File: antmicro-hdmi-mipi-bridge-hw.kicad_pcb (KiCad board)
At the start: 4 copper layers, 68 x 45 mm, 121 parts, among them IC1 TLV73325PDBVT, IC2 TLV73312PDBVT, IC3 TLV73325PDBVT, IC4 TLV73312PDBVT, J2 HDMI-A_Molex_471511001, J4 HDMI-A_Molex_471511001, J6 Conn_FFC_WE_68715014022, U1 TC358743XBG, U2 TPD8S009DSMR, U3 PCA9517ATP, U4 TC358743XBG, U5 TPD8S009DSMR, U6 PCA9517ATP, Y1 Oscillator_27MHz_TXC_7C, Y2 Oscillator_27MHz_TXC_7C

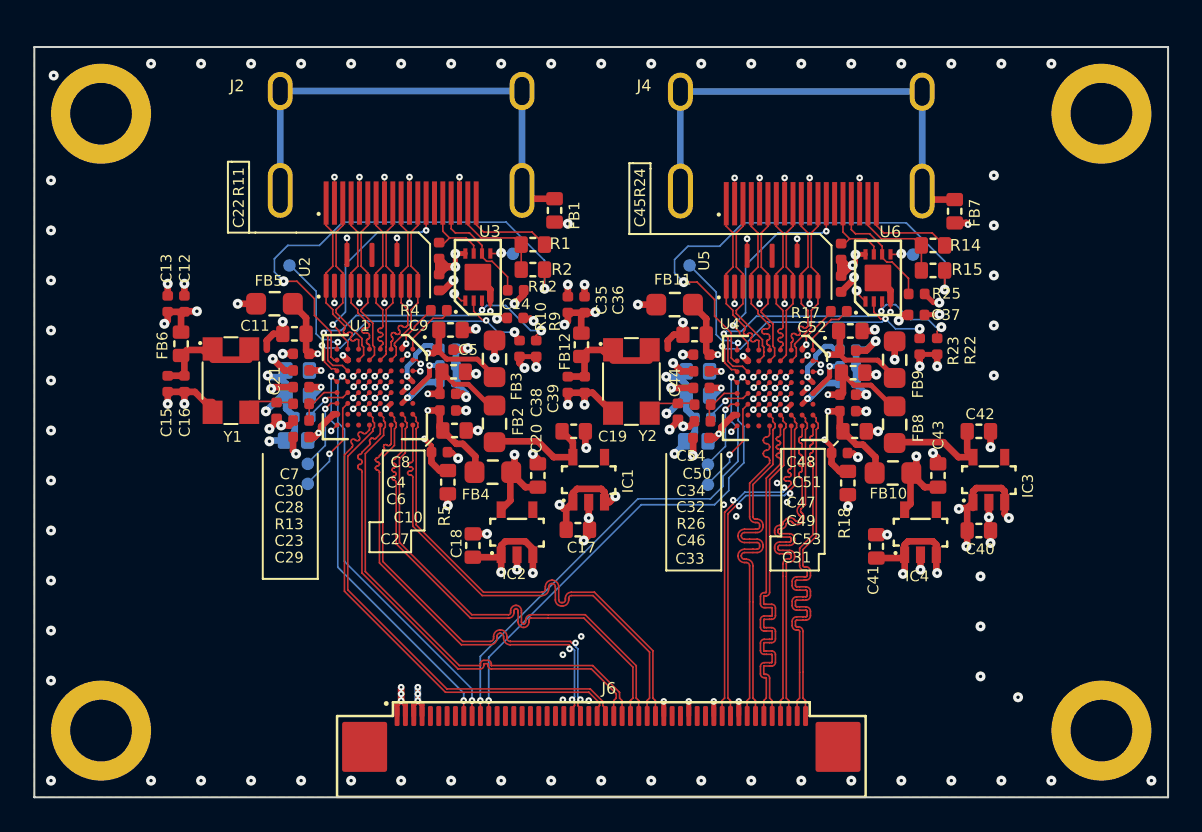
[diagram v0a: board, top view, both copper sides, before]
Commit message: Switch to micro-HDMI and widely-available parts for JLCPCB
- J2/J4: HDMI-A Molex 471511001 -> micro-HDMI (Type D) Molex 467651001,
  KiCad stock footprint. Symbol renumbered to the Type D pinout.
  D2/D0 fan out on F.Cu; D1/CLK drop to B.Cu via 0.15/0.30 mm vias in
  front of the inner pad row and rejoin the original routing, so the
  ESD-to-TC358743 routing is unchanged. Intra-pair skew re-matched to
  0.000 mm on all 8 pairs. DDC/HPD/CEC/5V re-routed for the new pinout.
- U3/U6: PCA9517ATP (HWSON8) -> PCA9517ADP (MSOP-8, same die), moved
  1.45 mm up into the space freed by the smaller connector.
- Y1/Y2: TXC 7C-27.000MBB-T -> HELE SSI027000E3CH; pads moved to the
  datasheet land (+-1.27 mm, previously +-1.9 mm).
- SP1-4: Wurth 9774060151R -> Sinhoo SMTSO2560CTJ; hole 3.7 -> 4.25 mm.
- IC2/IC4: TLV73312PDBVT -> TLV74312PDBVR (same pinout);
  IC1/IC3: TLV73325PDBVT -> TLV73325PDBVR (reel code).
- 470 pF, 4.7 uF, 2 k, 22 R: MPNs updated to in-stock equivalents.
- Design rules: min via diameter 0.40 -> 0.30 mm,
  min copper-to-edge clearance 0 -> 0.25 mm.

DRC: 0 unconnected, 0 schematic parity issues.

Co-Authored-By: Claude Opus 5.5 <noreply@anthropic.com>
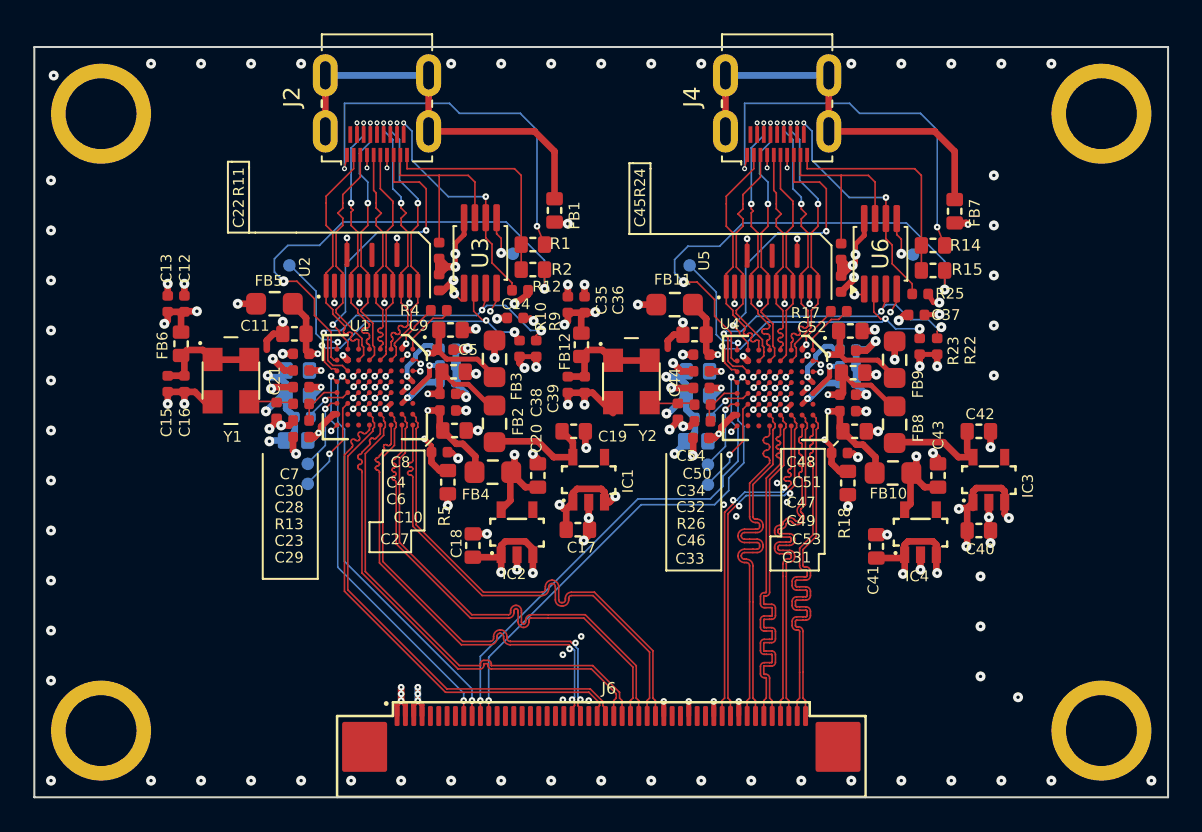
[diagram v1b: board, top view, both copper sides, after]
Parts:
- IC1, IC3: value TLV73325PDBVT -> TLV73325PDBVR
- IC2, IC4: value TLV73312PDBVT -> TLV74312PDBVR
- J2, J4: value HDMI-A_Molex_471511001 -> HDMI-D_Molex_467651001; footprint antmicro-footprints:HDMI-A_Receptacle_Molex_471511001 -> Connector_Video:HDMI_Micro-D_Molex_46765-1xxx
- SP1, SP2, SP3, SP4: value Spacer_Drill3.7mm_H6mm_9774060151R -> Spacer_Drill4.25mm_H6mm_SMTSO2560CTJ; footprint antmicro-footprints:Spacer_Drill3.7mm_H6mm_9774060151R -> antmicro-footprints:Spacer_Drill4.25mm_H6mm_SMTSO2560CTJ
- U3, U6: value PCA9517ATP -> PCA9517ADP; footprint antmicro-footprints:SOT1069-2 -> Package_SO:MSOP-8_3x3mm_P0.65mm
- Y1, Y2: value Oscillator_27MHz_TXC_7C -> Oscillator_27MHz_HELE_SSI027000E3CH
- moved J4 3.01 mm to (159.6, 91.7)
- moved J2 2.98 mm to (135.6, 91.7)
- moved U6 1.46 mm to (165.8, 102.4), turned to 90 degrees
- moved U3 1.46 mm to (141.8, 102.3), turned to 90 degrees
- moved R12 0.26 mm to (144.1, 104.6)
- moved R25 0.21 mm to (168.1, 104.8)
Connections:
- J2 pad 1: /Channel 1/HDMI1_D2_P -> /Channel 1/HDMI1_HPD
- J2 pad 10: /Channel 1/HDMI1_CLK_P -> GND
- J2 pad 11: GND -> /Channel 1/HDMI1_D0_N
- J2 pad 12: /Channel 1/HDMI1_CLK_N -> /Channel 1/HDMI1_CLK_P
- J2 pad 13: /Channel 1/HDMI1_CEC -> GND
- J2 pad 14: /Channel 1/DUMMY1 -> /Channel 1/HDMI1_CLK_N
- J2 pad 15: /Channel 1/HDMI1_DDC_SCL -> /Channel 1/HDMI1_CEC
- J2 pad 16: /Channel 1/HDMI1_DDC_SDA -> GND
- J2 pad 17: GND -> /Channel 1/HDMI1_DDC_SCL
- J2 pad 18: /Channel 1/HDMI1_POWER -> /Channel 1/HDMI1_DDC_SDA
- J2 pad 19: /Channel 1/HDMI1_HPD -> /Channel 1/HDMI1_POWER
- J2 pad 2: GND -> /Channel 1/DUMMY1
- J2 pad 3: /Channel 1/HDMI1_D2_N -> /Channel 1/HDMI1_D2_P
- J2 pad 4: /Channel 1/HDMI1_D1_P -> GND
- J2 pad 5: GND -> /Channel 1/HDMI1_D2_N
- J2 pad 6: /Channel 1/HDMI1_D1_N -> /Channel 1/HDMI1_D1_P
- J2 pad 7: /Channel 1/HDMI1_D0_P -> GND
- J2 pad 8: GND -> /Channel 1/HDMI1_D1_N
- J2 pad 9: /Channel 1/HDMI1_D0_N -> /Channel 1/HDMI1_D0_P
- J4 pad 1: /Channel 2/HDMI2_D2_P -> /Channel 2/HDMI2_HPD
- J4 pad 10: /Channel 2/HDMI2_CLK_P -> GND
- J4 pad 11: GND -> /Channel 2/HDMI2_D0_N
- J4 pad 12: /Channel 2/HDMI2_CLK_N -> /Channel 2/HDMI2_CLK_P
- J4 pad 13: /Channel 2/HDMI2_CEC -> GND
- J4 pad 14: /Channel 2/DUMMY2 -> /Channel 2/HDMI2_CLK_N
- J4 pad 15: /Channel 2/HDMI2_DDC_SCL -> /Channel 2/HDMI2_CEC
- J4 pad 16: /Channel 2/HDMI2_DDC_SDA -> GND
- J4 pad 17: GND -> /Channel 2/HDMI2_DDC_SCL
- J4 pad 18: /Channel 2/HDMI2_POWER -> /Channel 2/HDMI2_DDC_SDA
- J4 pad 19: /Channel 2/HDMI2_HPD -> /Channel 2/HDMI2_POWER
- J4 pad 2: GND -> /Channel 2/DUMMY2
- J4 pad 3: /Channel 2/HDMI2_D2_N -> /Channel 2/HDMI2_D2_P
- J4 pad 4: /Channel 2/HDMI2_D1_P -> GND
- J4 pad 5: GND -> /Channel 2/HDMI2_D2_N
- J4 pad 6: /Channel 2/HDMI2_D1_N -> /Channel 2/HDMI2_D1_P
- J4 pad 7: /Channel 2/HDMI2_D0_P -> GND
- J4 pad 8: GND -> /Channel 2/HDMI2_D1_N
- J4 pad 9: /Channel 2/HDMI2_D0_N -> /Channel 2/HDMI2_D0_P
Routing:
- net /Channel 2/HDMI2_HPD: track 5.89 -> 24.0 mm, vias 0 -> 2
- net /Channel 1/HDMI1_HPD: track 5.89 -> 23.9 mm, vias 0 -> 2
- net /Channel 2/HDMI2_DDC_SDA: track 7.16 -> 14.9 mm, vias 0 -> 2
- net /Channel 1/HDMI1_DDC_SDA: track 7.13 -> 14.7 mm, vias 0 -> 2
- net /Channel 2/HDMI2_DDC_SCL: track 5.09 -> 12.1 mm
- net /Channel 2/HDMI2_POWER: track 6.49 -> 13.5 mm
- net /Channel 1/HDMI1_POWER: track 6.49 -> 13.5 mm
- net /Channel 1/HDMI1_DDC_SCL: track 5.09 -> 12.0 mm
- net /Channel 2/HDMI2_CLK_N: track 10.5 -> 16.7 mm, vias 0 -> 2
- net /Channel 2/HDMI2_CLK_P: track 10.4 -> 16.7 mm, vias 0 -> 2
- net /Channel 1/HDMI1_CLK_N: track 10.5 -> 16.7 mm, vias 0 -> 2
- net /Channel 1/HDMI1_CLK_P: track 10.4 -> 16.6 mm, vias 0 -> 2
- net /Channel 2/HDMI2_D1_N: track 10.4 -> 16.4 mm, vias 0 -> 2
- net /Channel 1/HDMI1_D1_N: track 10.4 -> 16.4 mm, vias 0 -> 2
- net /Channel 2/HDMI2_D1_P: track 10.4 -> 16.4 mm, vias 0 -> 2
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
